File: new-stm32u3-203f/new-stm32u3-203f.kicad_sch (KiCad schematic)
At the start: 36 parts, among them J1 DM3CS-SF, J2 SJ-3524-SMT, J3 12401826E412A, SW1 SW_SPDT, U1 STM32U385RGT6Q, U2 TLV320DAC3203IRGER, X1 32.768kHz

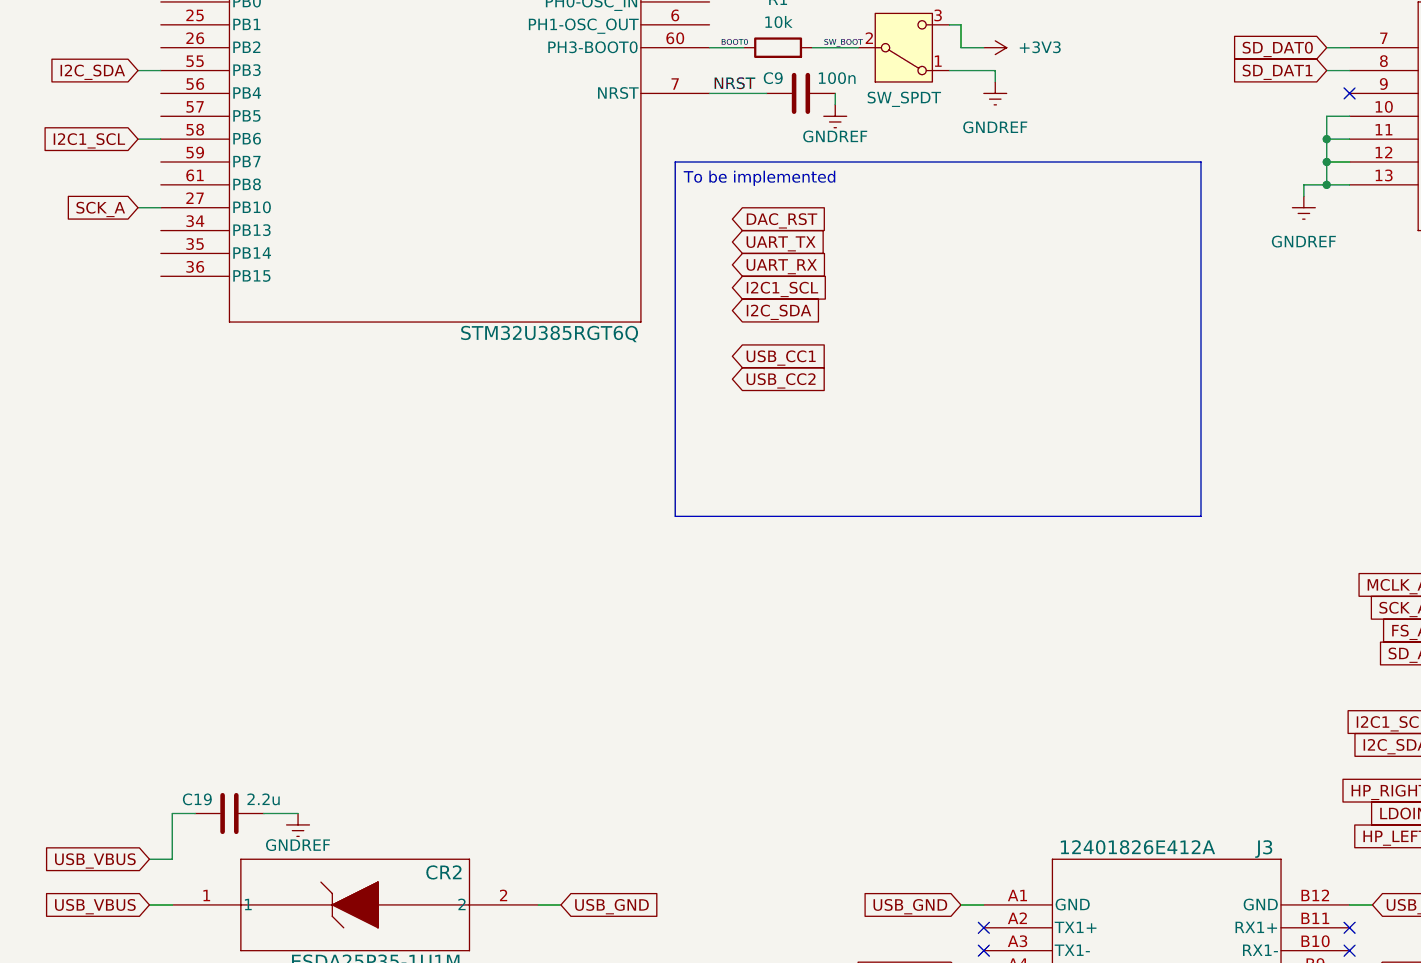
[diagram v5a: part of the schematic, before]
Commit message: finished the USB page of the eval board. now need to do power for 3v3, 5v, & 1v8
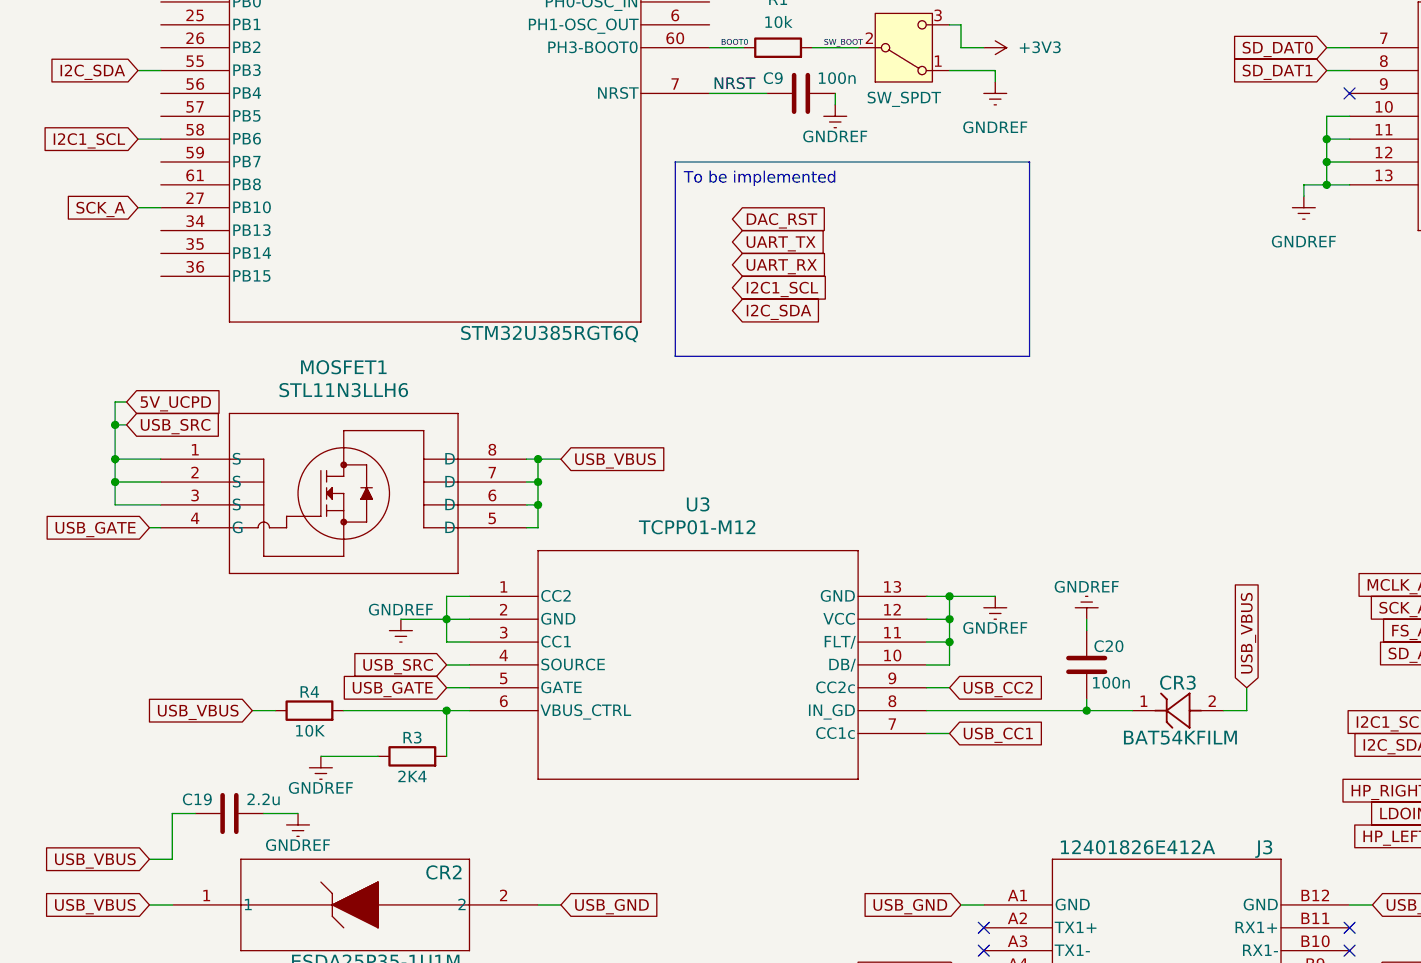
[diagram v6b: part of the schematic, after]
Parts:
- added C20: 100n, symbol Device:C
- added CR3: BAT54KFILM, SOD-523_STM, symbol 2026-01-26_03-59-16:BAT54KFILM
- added MOSFET1: STL11N3LLH6, POWERFLAT-3p3X3p3_STM, symbol 2026-01-26_04-02-48:STL11N3LLH6
- added R3: 2K4, symbol Device:R
- added R4: 10K, symbol Device:R
- added U3: TCPP01-M12, QFN12_TCPP01-M12_STM, symbol 2026-01-26_03-34-42:TCPP01-M12
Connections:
- net GNDREF: now also C20.2, R3.1, U3.1 (CC2), U3.10 (DB/), U3.11 (FLT/), U3.12 (VCC), U3.13 (GND), U3.2 (GND), U3.3 (CC1)
- net USB_CC1: now also U3.7 (CC1c)
- net USB_CC2: now also U3.9 (CC2c)
- net USB_VBUS: now also CR3.2, MOSFET1.5 (D), MOSFET1.6 (D), MOSFET1.7 (D), MOSFET1.8 (D), R4.1
- new net: R3.2, R4.2, U3.6 (VBUS_CTRL)
- new net: C20.1, CR3.1, U3.8 (IN_GD)
- new net 5V_UCPD: MOSFET1.1 (S), MOSFET1.2 (S), MOSFET1.3 (S), U3.4 (SOURCE)
- new net USB_GATE: MOSFET1.4 (G), U3.5 (GATE)

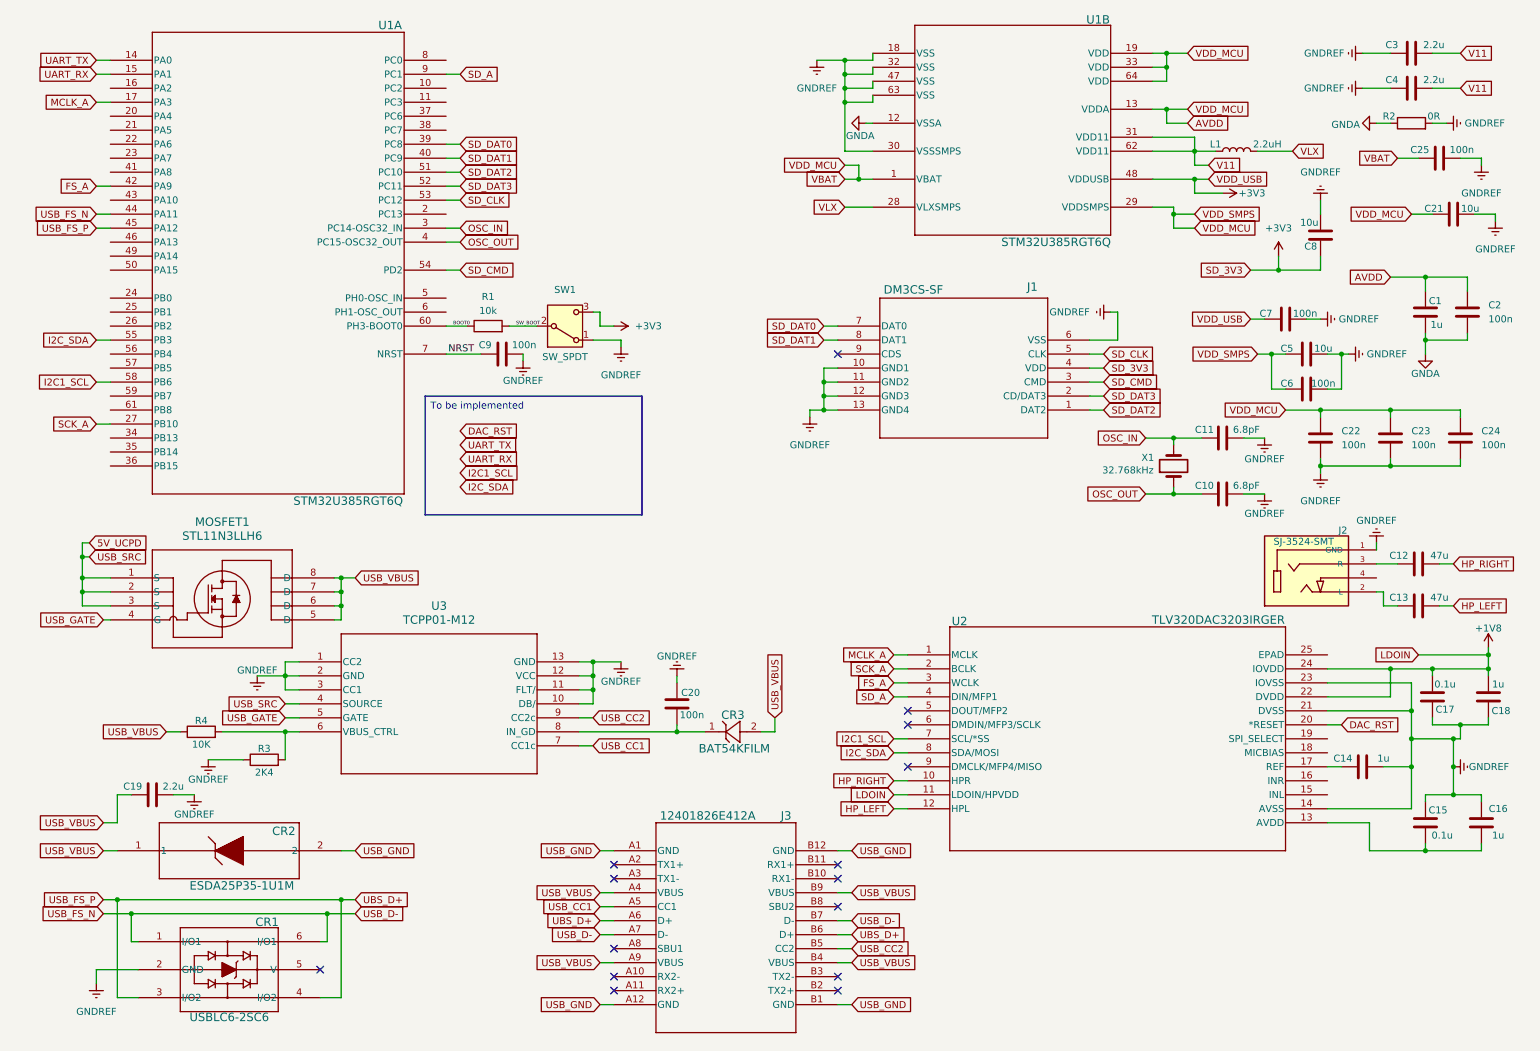
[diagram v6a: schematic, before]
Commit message: added 1v8 power
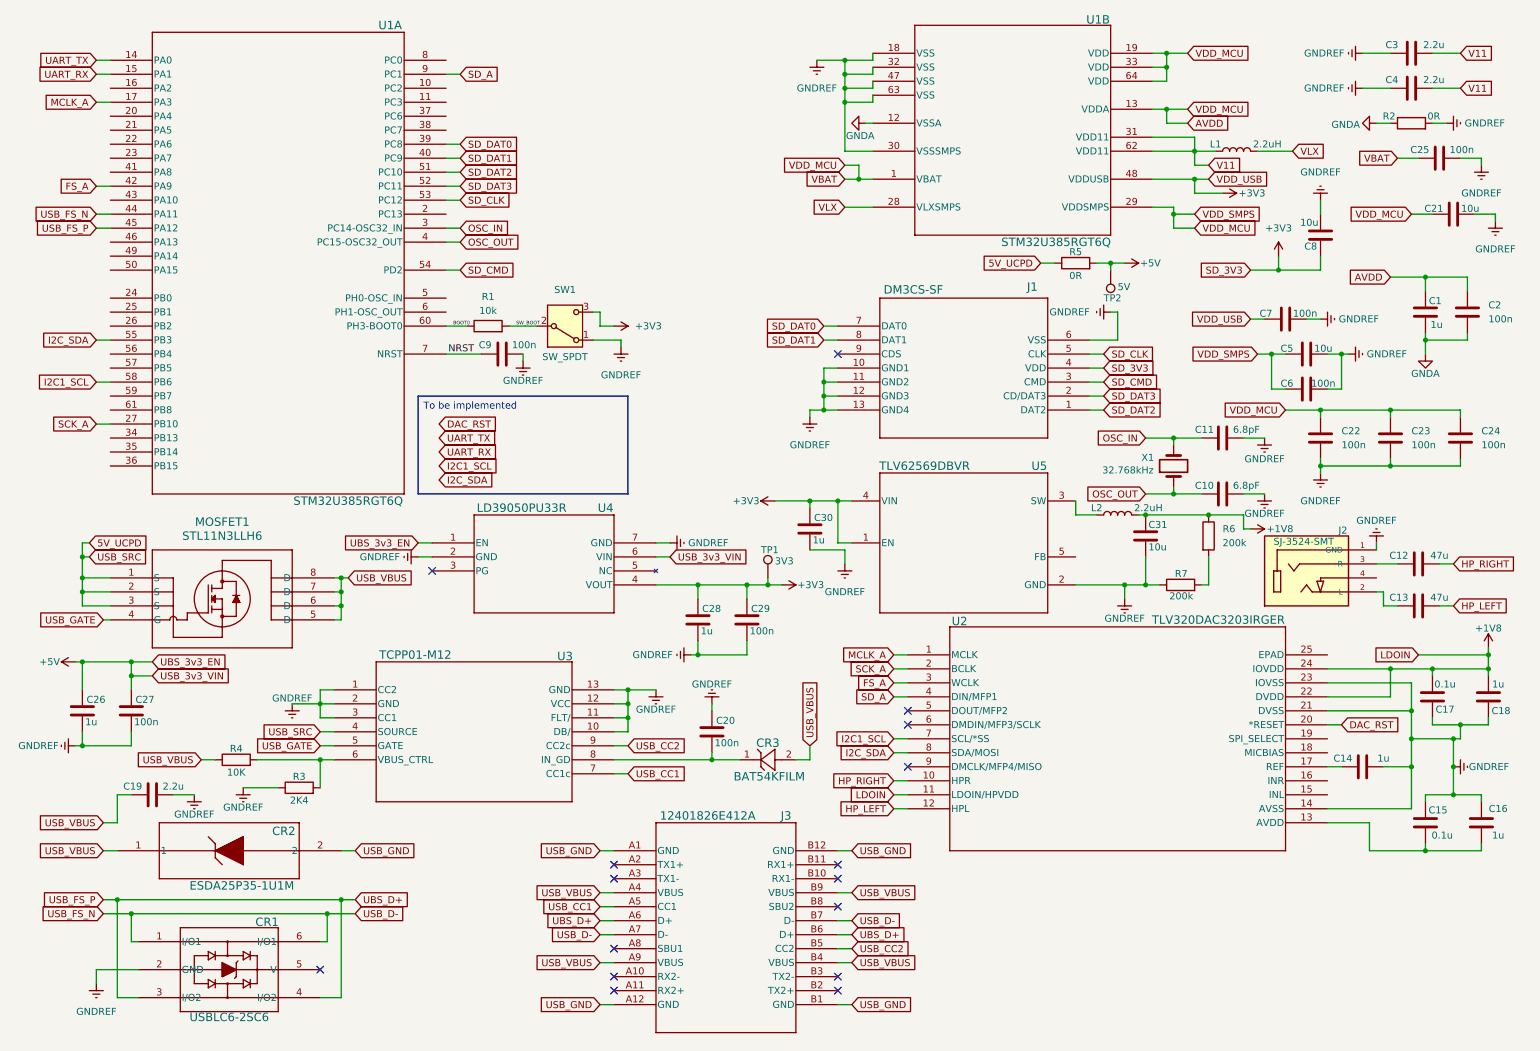
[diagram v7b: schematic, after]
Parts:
- added C26, C28, C30: 1u, symbol Device:C
- added C27, C29: 100n, symbol Device:C
- added C31: 10u, symbol Device:C
- added L2: 2.2uH, symbol Device:L
- added R5: 0R, symbol Device:R
- added R6, R7: 200k, symbol Device:R
- added TP1: 3V3, symbol Connector:TestPoint
- added TP2: 5V, symbol Connector:TestPoint
- added U4: LD39050PU33R, DFN6_3X3_STM, symbol 2026-01-26_04-25-52:LD39050PU33R
- added U5: TLV62569DBVR, DBV0005A_N, symbol 2026-01-26_07-03-52:TLV62569DBVR
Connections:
- net +1V8: now also C31.2, L2.2, R6.1
- net +3V3: now also C28.2, C29.2, C30.2, TP1.1, U4.4 (VOUT), U5.1 (EN), U5.4 (VIN)
- net 5V_UCPD: now also R5.1
- net GNDREF: now also C26.1, C27.1, C28.1, C29.1, C30.1, C31.1, R7.1, U4.2 (GND), U4.7 (GND), U5.2 (GND)
- new net: L2.1, U5.3 (SW)
- new net: R6.2, R7.2
- new net +5V: C26.2, C27.2, R5.2, TP2.1, U4.1 (EN), U4.6 (VIN)
- no-connect marks 15 -> 16
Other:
- moved on the sheet: C20, CR3, R3, R4, U3

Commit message: moved some studd around.
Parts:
- added TP3: 1V8, symbol Connector:TestPoint
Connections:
- net +1V8: now also TP3.1
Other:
- moved on the sheet: J2, SW1
